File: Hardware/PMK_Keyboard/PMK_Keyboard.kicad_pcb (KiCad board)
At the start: 2 copper layers, 174 x 153 mm, 52 parts, among them IC1 SN74HC165PWR, IC2 SN74HC165PWR, IC3 SN74HC165PWR, IC4 SN74HC165PWR, IC5 SN74HC165PWR, IC7 ESP32-S2FH4, SW1 SW_Push, SW10 SW_Push, SW11 SW_Push, SW12 SW_Push, SW13 SW_Push, SW14 SW_Push, SW15 SW_Push, SW16 SW_Push, SW17 SW_Push, SW18 SW_Push, SW19 SW_Push, SW2 SW_Push, SW20 SW_Push, SW21 SW_Push, SW22 SW_Push, SW23 SW_Push, SW24 SW_Push, SW25 SW_Push, SW26 SW_Push, SW27 SW_Push, SW28 SW_Push, SW29 SW_Push, SW3 SW_Push, SW30 SW_Push, SW31 SW_Push, SW32 SW_Push, SW33 SW_Push, SW34 SW_Push, SW35 SW_Push, SW36 SW_Push, SW37 SW_Push, SW38 SW_Push, SW39 SW_Push, SW4 SW_Push, SW40 SW_Push, SW5 SW_Push, SW6 SW_Push, SW7 SW_Push, SW8 SW_Push, SW9 SW_Push

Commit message: yay routing to switches is done
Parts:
- moved SW33 40.0 mm to (162.0, 143.0)
- moved SW34 35.8 mm to (160.0, 183.0)
- moved SW23 22.0 mm to (32.0, 129.0)
- moved SW24 22.0 mm to (54.0, 129.0)
- moved SW36 18.4 mm to (178.0, 152.0)
- moved RN5 9.96 mm to (172.0, 125.2), turned to 180 degrees
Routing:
- net /8: track 0.00 -> 168.3 mm
- net /16: track 8.42 -> 147.3 mm
- net /7: track 8.42 -> 146.3 mm
- net /15: track 8.42 -> 145.6 mm
- net /23: track 8.42 -> 145.1 mm
- net /24: track 8.42 -> 122.3 mm
- net /14: track 8.25 -> 120.0 mm
- net /22: track 8.25 -> 119.3 mm
- net /6: track 8.42 -> 117.1 mm
- net /21: track 8.42 -> 106.5 mm
- net /13: track 8.42 -> 106.1 mm
- net /5: track 8.25 -> 105.6 mm
- net /CLK: track 90.2 -> 0.00 mm
- net /4: track 8.25 -> 90.1 mm
- net /20: track 8.42 -> 89.2 mm
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
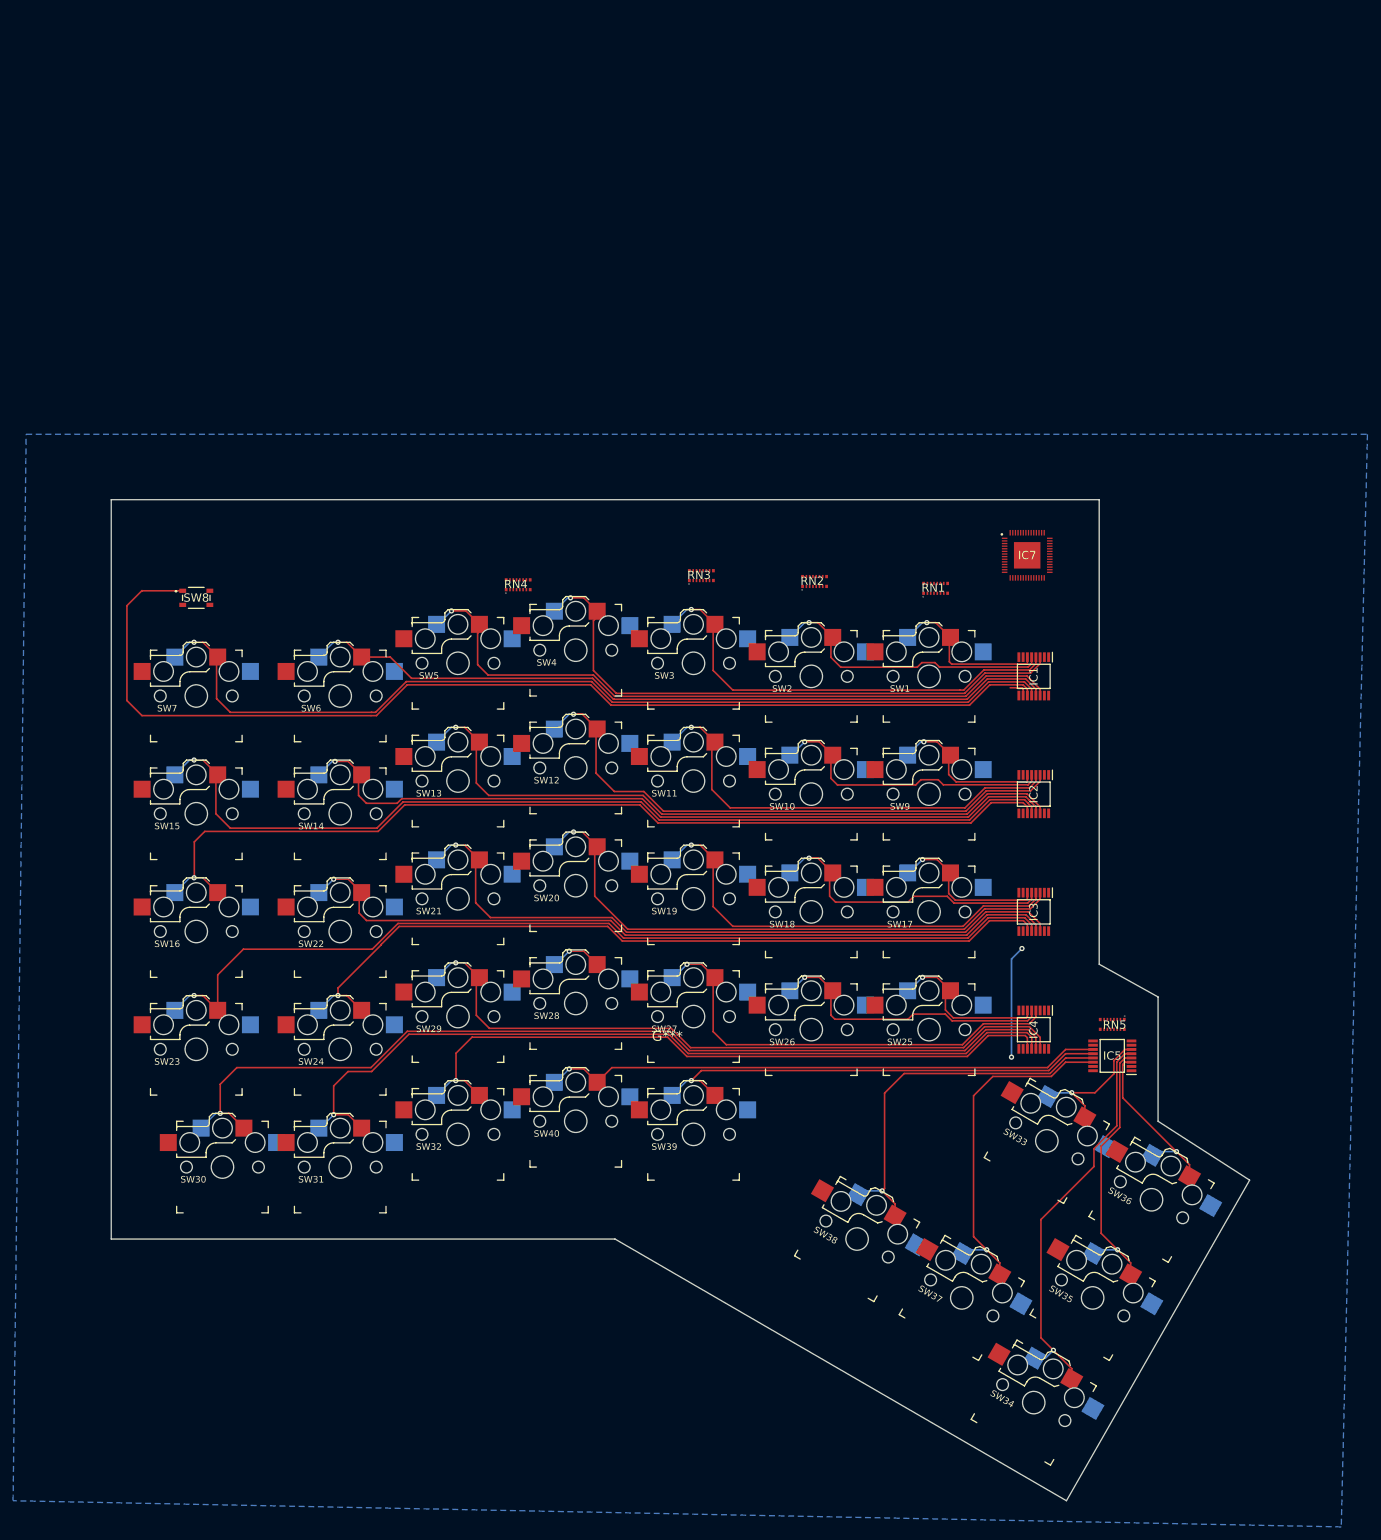
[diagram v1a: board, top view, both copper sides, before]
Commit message: Redone routing for 180mm version
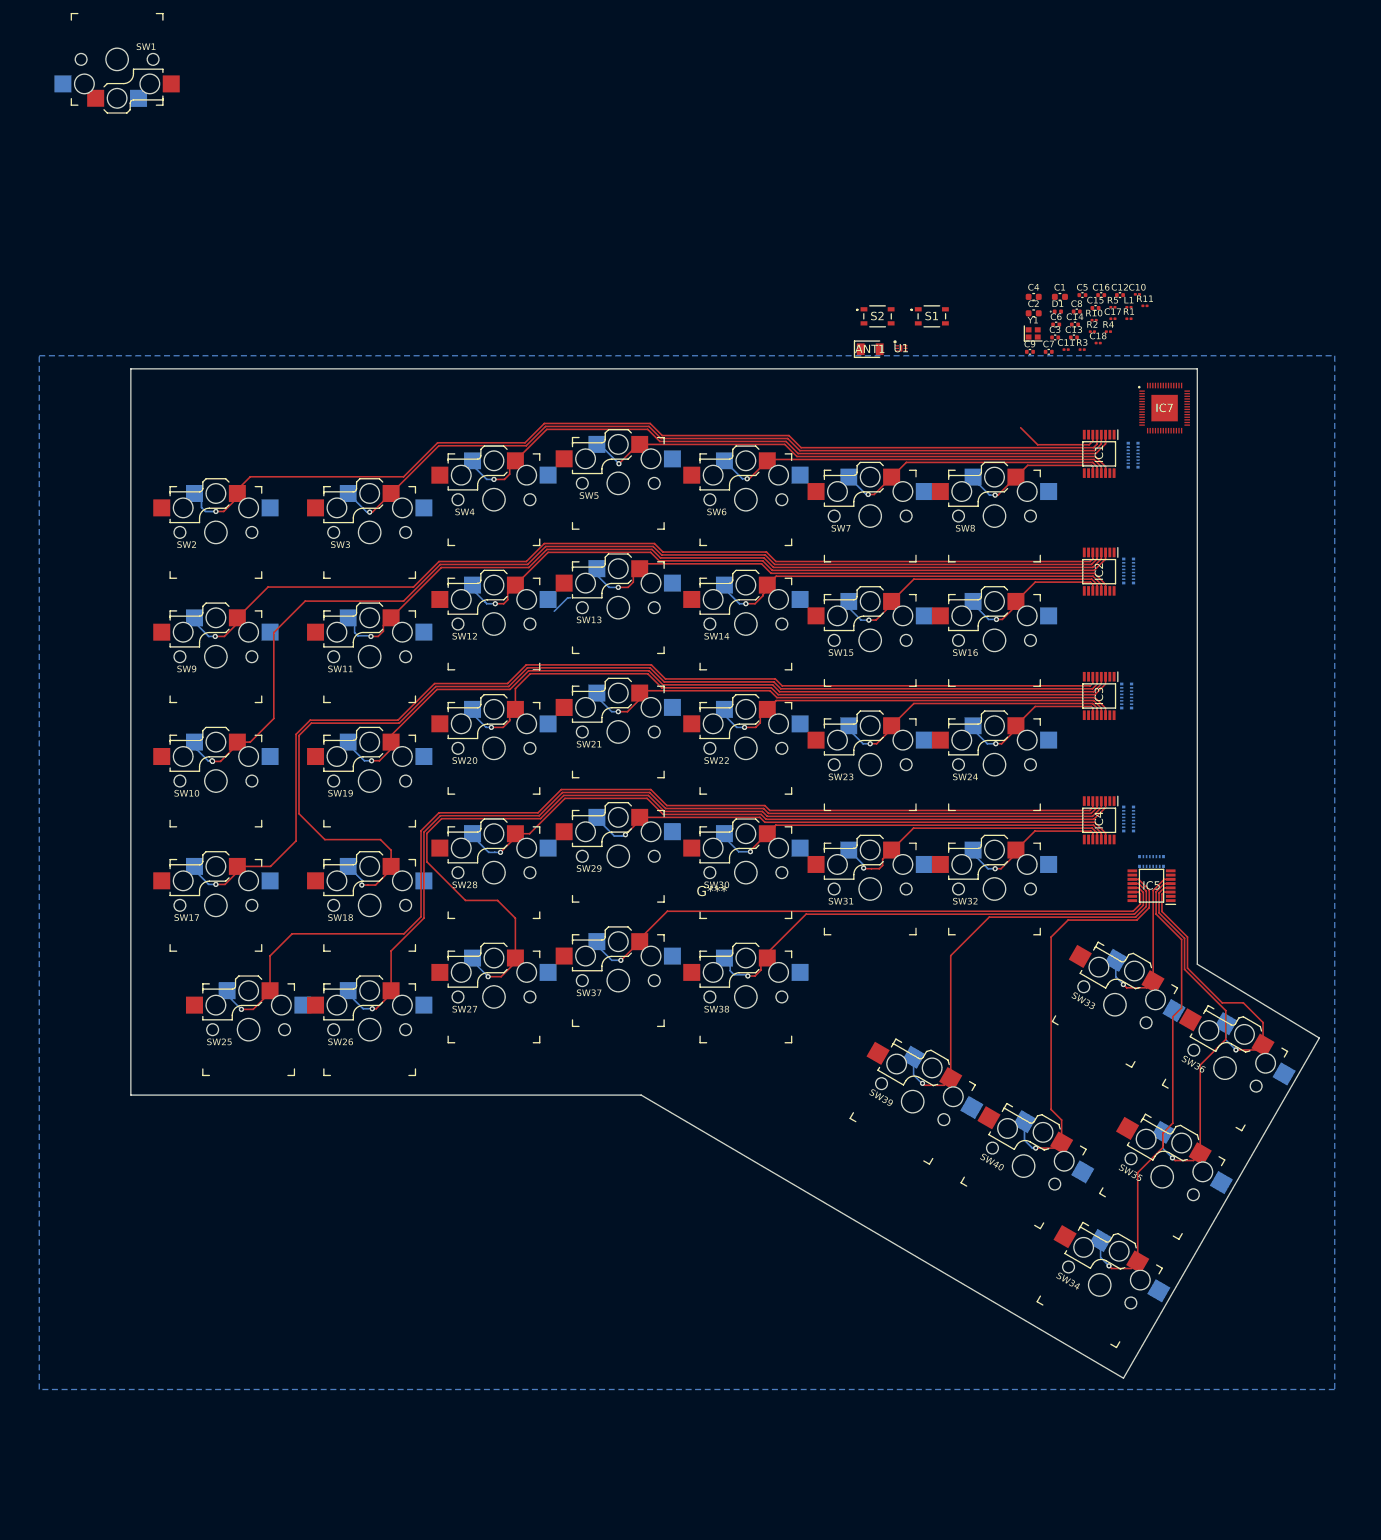
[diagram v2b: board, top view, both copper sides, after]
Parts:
- removed the G*** at (104.0, 127.0)
- added ANT1: 2450AT18A100E, Component_lib:ANTC3216X140N, F.Cu at (135.0, 22.0)
- added C1: 10u, Capacitor_SMD:C_0603_1608Metric, F.Cu at (164.0, 14.0)
- added C10: 15p, Capacitor_SMD:C_0201_0603Metric, F.Cu at (175.8, 13.6)
- added C11: 15p, Capacitor_SMD:C_0201_0603Metric, F.Cu at (164.9, 22.1)
- added C12: 100n, Capacitor_SMD:C_0402_1005Metric, F.Cu at (173.2, 13.7)
- added C13: 100n, Capacitor_SMD:C_0402_1005Metric, F.Cu at (166.1, 20.2)
- added C14: 100n, Capacitor_SMD:C_0402_1005Metric, F.Cu at (166.3, 18.2)
- added C15: 1u, Capacitor_SMD:C_0402_1005Metric, F.Cu at (169.4, 15.7)
- added C16: 100n, Capacitor_SMD:C_0402_1005Metric, F.Cu at (170.3, 13.7)
- added C17: C, Capacitor_SMD:C_0201_0603Metric, F.Cu at (172.1, 17.3)
- added C18: C, Capacitor_SMD:C_0201_0603Metric, F.Cu at (169.8, 21.1)
- added C2: 10u, Capacitor_SMD:C_0603_1608Metric, F.Cu at (160.0, 16.5)
- added C3: 100n, Capacitor_SMD:C_0402_1005Metric, F.Cu at (163.3, 20.2)
- added C4: 10u, Capacitor_SMD:C_0603_1608Metric, F.Cu at (160.0, 14.0)
- added C5: 100n, Capacitor_SMD:C_0402_1005Metric, F.Cu at (167.4, 13.7)
- added C6: 1u, Capacitor_SMD:C_0402_1005Metric, F.Cu at (163.4, 18.2)
- added C7: 100n, Capacitor_SMD:C_0402_1005Metric, F.Cu at (162.3, 22.4)
- added C8: 100n, Capacitor_SMD:C_0402_1005Metric, F.Cu at (166.6, 16.2)
- added C9: 100n, Capacitor_SMD:C_0402_1005Metric, F.Cu at (159.4, 22.4)
- added D1: LED, LED_SMD:LED_0402_1005Metric, F.Cu at (163.7, 16.2)
- added G***: LOGO, Component_lib:pmk-v1-noFN_180mm, F.Cu at (110.8, 104.9)
- added L1: L, Inductor_SMD:L_0201_0603Metric, F.Cu at (174.6, 15.6)
- added R1: 0k, Resistor_SMD:R_0201_0603Metric, F.Cu at (174.6, 17.3)
- added R10: 5.1k, Resistor_SMD:R_0201_0603Metric, F.Cu at (169.2, 17.6)
- added R11: 5.1k, Resistor_SMD:R_0201_0603Metric, F.Cu at (177.0, 15.4)
- added R2: 0, Resistor_SMD:R_0201_0603Metric, F.Cu at (169.0, 19.3)
- added R3: 10k, Resistor_SMD:R_0201_0603Metric, F.Cu at (167.4, 22.1)
- added R4: 2k, Resistor_SMD:R_0201_0603Metric, F.Cu at (171.4, 19.3)
- added R5: 10k, Resistor_SMD:R_0201_0603Metric, F.Cu at (172.1, 15.6)
- added S1: SKRPABE010, Component_lib:SKRPABE010, F.Cu at (144.4, 17.0)
- added S2: SKRPABE010, Component_lib:SKRPABE010, F.Cu at (136.1, 17.0)
- added U1: MIC5528-3.3YMT-T5, Component_lib:SON40P120X120X60-7N-D, F.Cu at (139.8, 21.9)
- added Y1: 40MHz, Component_lib:Crystal_SMD_2016-4Pin_2.0x1.6mm, F.Cu at (159.9, 19.6)
- RN1, RN2, RN3, RN4, RN5: moved to B.Cu
- SW8: footprint Component_lib:SKRPABE010 -> Component_lib:Kailh_socket_PG1350_reversible
- moved SW1 155.9 mm to (19.9, -22.3), turned to 0 degrees
- moved SW16 129.9 mm to (154.0, 66.5)
- moved SW8 122.6 mm to (154.0, 47.5), turned to 180 degrees
- moved SW23 111.8 mm to (135.0, 85.5)
- moved SW9 111.0 mm to (35.0, 69.0)
- moved SW24 109.1 mm to (154.0, 85.5)
- moved SW17 109.0 mm to (35.0, 107.0)
- moved SW7 106.6 mm to (135.0, 47.5)
- moved SW15 106.4 mm to (135.0, 66.5)
- moved SW25 104.0 mm to (40.0, 126.0)
- moved RN4 99.9 mm to (174.5, 93.8), turned to -90 degrees
- moved SW2 93.6 mm to (35.0, 50.0)
- moved SW30 91.8 mm to (116.0, 102.0)
- moved SW31 91.5 mm to (135.0, 104.5)
- moved SW10 91.0 mm to (35.0, 88.0)
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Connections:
- net /CLK renamed /SPI_CLK
- net /MISO renamed /SPI_MISO
- IC7 pad 1: unconnected-(IC7-Pad1) -> +3V3
- IC7 pad 10: unconnected-(IC7-Pad10) -> /IO5
- IC7 pad 11: unconnected-(IC7-Pad11) -> /IO6
- IC7 pad 12: unconnected-(IC7-Pad12) -> /IO7
- IC7 pad 13: unconnected-(IC7-Pad13) -> /IO8
- IC7 pad 14: unconnected-(IC7-Pad14) -> /IO9
- IC7 pad 15: unconnected-(IC7-Pad15) -> /IO10
- IC7 pad 16: unconnected-(IC7-Pad16) -> /IO11
- IC7 pad 17: unconnected-(IC7-Pad17) -> /IO12
- IC7 pad 18: unconnected-(IC7-Pad18) -> /IO13
- IC7 pad 19: unconnected-(IC7-Pad19) -> /IO14
- IC7 pad 2: unconnected-(IC7-Pad2) -> /LNA_IN
- IC7 pad 20: unconnected-(IC7-Pad20) -> +3V3
- IC7 pad 21: unconnected-(IC7-Pad21) -> /IO15
- IC7 pad 22: unconnected-(IC7-Pad22) -> /IO16
- IC7 pad 23: unconnected-(IC7-Pad23) -> /IO17
- IC7 pad 24: unconnected-(IC7-Pad24) -> /IO18
- IC7 pad 25: unconnected-(IC7-Pad25) -> /D-
- IC7 pad 26: unconnected-(IC7-Pad26) -> /D+
- IC7 pad 27: unconnected-(IC7-Pad27) -> +3V3
- IC7 pad 28: unconnected-(IC7-Pad28) -> /IO21
- IC7 pad 3: unconnected-(IC7-Pad3) -> +3V3
- IC7 pad 30: unconnected-(IC7-Pad30) -> /VDD_SPI
- IC7 pad 37: unconnected-(IC7-Pad37) -> /IO33
- IC7 pad 38: unconnected-(IC7-Pad38) -> /IO34
- IC7 pad 39: unconnected-(IC7-Pad39) -> /IO35
- IC7 pad 4: unconnected-(IC7-Pad4) -> +3V3
- IC7 pad 40: unconnected-(IC7-Pad40) -> /IO36
- IC7 pad 41: unconnected-(IC7-Pad41) -> /IO37
- IC7 pad 42: unconnected-(IC7-Pad42) -> /IO38
- IC7 pad 43: unconnected-(IC7-Pad43) -> /IO39
- IC7 pad 44: unconnected-(IC7-Pad44) -> /IO40
- IC7 pad 45: unconnected-(IC7-Pad45) -> +3V3
- IC7 pad 46: unconnected-(IC7-Pad46) -> /IO41
- IC7 pad 47: unconnected-(IC7-Pad47) -> /IO42
- IC7 pad 48: unconnected-(IC7-Pad48) -> /IO43
- IC7 pad 49: unconnected-(IC7-Pad49) -> /IO44
- IC7 pad 5: unconnected-(IC7-Pad5) -> /IO0
- IC7 pad 50: unconnected-(IC7-Pad50) -> /IO45
- IC7 pad 51: unconnected-(IC7-Pad51) -> +3V3
- IC7 pad 52: unconnected-(IC7-Pad52) -> Net-(IC7-Pad52)
- IC7 pad 53: unconnected-(IC7-Pad53) -> Net-(IC7-Pad53)
- IC7 pad 54: unconnected-(IC7-Pad54) -> +3V3
- IC7 pad 55: unconnected-(IC7-Pad55) -> /IO46
- IC7 pad 56: unconnected-(IC7-Pad56) -> /EN
- IC7 pad 57: unconnected-(IC7-Pad57) -> GND
- IC7 pad 6: unconnected-(IC7-Pad6) -> /IO1
- IC7 pad 7: unconnected-(IC7-Pad7) -> /IO2
- IC7 pad 8: unconnected-(IC7-Pad8) -> /IO3
- IC7 pad 9: unconnected-(IC7-Pad9) -> /IO4
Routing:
- net /8: track 168.3 -> 21.8 mm, vias 0 -> 1
- net /17: track 25.0 -> 165.2 mm
- net /25: track 25.6 -> 161.3 mm
- net /18: track 45.4 -> 169.5 mm
- net /16: track 147.3 -> 23.5 mm
- net /9: track 24.8 -> 147.6 mm
- net /10: track 44.9 -> 163.6 mm, vias 1 -> 2
- net /2: track 44.7 -> 149.2 mm
- net /7: track 146.3 -> 42.3 mm
- net /15: track 145.6 -> 43.9 mm
- net /23: track 145.1 -> 43.6 mm
- net /26: track 45.0 -> 143.8 mm
- net /24: track 122.3 -> 23.7 mm
- net /28: track 8.25 -> 105.0 mm
- net /31: track 127.2 -> 43.8 mm
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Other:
- board size 174 x 153 mm -> 181.6 x 154.3 mm

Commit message: Started routing the pullups
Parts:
- moved RN1 2.71 mm to (172.5, 38.0)
- moved RN4 2.01 mm to (172.5, 94.0)
- moved RN2 2.00 mm to (172.5, 55.9)
- moved RN3 1.70 mm to (172.5, 75.0)
- moved RN5 1.20 mm to (178.0, 101.5), turned to 0 degrees
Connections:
- RN1 pad 10: /7 -> /6
- RN1 pad 11: /6 -> /7
- RN1 pad 12: /5 -> /8
- RN1 pad 13: /4 -> /1
- RN1 pad 14: /3 -> /2
- RN1 pad 15: /2 -> /3
- RN1 pad 16: /1 -> /4
- RN1 pad 9: /8 -> /5
- RN2 pad 10: /15 -> /14
- RN2 pad 11: /14 -> /15
- RN2 pad 12: /13 -> /16
- RN2 pad 13: /12 -> /9
- RN2 pad 14: /11 -> /10
- RN2 pad 15: /10 -> /11
- RN2 pad 16: /9 -> /12
- RN2 pad 9: /16 -> /13
- RN3 pad 10: /23 -> /22
- RN3 pad 11: /22 -> /23
- RN3 pad 12: /21 -> /24
- RN3 pad 13: /20 -> /17
- RN3 pad 14: /19 -> /18
- RN3 pad 15: /18 -> /19
- RN3 pad 16: /17 -> /20
- RN3 pad 9: /24 -> /21
- RN4 pad 10: /31 -> /30
- RN4 pad 11: /30 -> /31
- RN4 pad 12: /29 -> /32
- RN4 pad 13: /28 -> /25
- RN4 pad 14: /27 -> /26
- RN4 pad 15: /26 -> /27
- RN4 pad 16: /25 -> /28
- RN4 pad 9: /32 -> /29
- RN5 pad 10: /39 -> /38
- RN5 pad 11: /38 -> /39
- RN5 pad 12: /37 -> /40
- RN5 pad 13: /36 -> /33
- RN5 pad 14: /35 -> /34
- RN5 pad 15: /34 -> /35
- RN5 pad 16: /33 -> /36
- RN5 pad 9: /40 -> /37
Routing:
- net /10: track 163.6 -> 172.8 mm, vias 2 -> 3
- net /15: track 43.9 -> 52.9 mm, vias 1 -> 2
- net /2: track 149.2 -> 158.1 mm, vias 1 -> 2
- net /1: track 13.3 -> 22.0 mm, vias 0 -> 1
- net /11: track 125.7 -> 134.3 mm, vias 1 -> 2
- net /7: track 42.3 -> 50.7 mm, vias 1 -> 2
- net /14: track 62.9 -> 71.1 mm, vias 1 -> 2
- net /16: track 23.5 -> 31.4 mm, vias 1 -> 2
- net /3: track 125.1 -> 132.7 mm, vias 1 -> 2
- net /6: track 61.4 -> 69.0 mm, vias 1 -> 2
- net /9: track 147.6 -> 155.0 mm, vias 1 -> 2
- net /8: track 21.8 -> 28.8 mm, vias 1 -> 2
- net /13: track 83.9 -> 89.4 mm, vias 1 -> 2
- net /12: track 105.1 -> 110.2 mm, vias 1 -> 2
- net /20: track 107.2 -> 112.2 mm, vias 1 -> 2
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
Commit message: Keyboard routing is ongoing
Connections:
- RN5 pad 10: /38 -> /34
- RN5 pad 11: /39 -> /35
- RN5 pad 12: /40 -> /36
- RN5 pad 13: /33 -> /37
- RN5 pad 14: /34 -> /38
- RN5 pad 15: /35 -> /39
- RN5 pad 16: /36 -> /40
- RN5 pad 9: /37 -> /33
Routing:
- net /SPI_CLK: track 0.00 -> 149.3 mm, vias 0 -> 5
- net /PL: track 0.00 -> 131.8 mm, vias 0 -> 5
- net /CE: track 0.00 -> 129.7 mm, vias 0 -> 5
- net +3V3: track 0.00 -> 86.6 mm, vias 0 -> 6
- net /3-4: track 0.00 -> 22.0 mm, vias 0 -> 2
- net /2-3: track 0.00 -> 21.9 mm, vias 0 -> 2
- net /1-2: track 0.00 -> 20.8 mm, vias 0 -> 2
- net /4-5: track 0.00 -> 11.6 mm
- net /31: track 43.8 -> 53.8 mm, vias 1 -> 2
- net /35: track 55.1 -> 65.0 mm, vias 1 -> 2
- net /23: track 43.6 -> 53.4 mm, vias 1 -> 2
- net /38: track 77.4 -> 86.6 mm, vias 1 -> 2
- net /26: track 145.1 -> 154.3 mm, vias 1 -> 2
- net /18: track 169.5 -> 178.7 mm, vias 1 -> 2
- net /37: track 93.0 -> 102.2 mm, vias 1 -> 2
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- removed copper zone on B.Cu, net GND
